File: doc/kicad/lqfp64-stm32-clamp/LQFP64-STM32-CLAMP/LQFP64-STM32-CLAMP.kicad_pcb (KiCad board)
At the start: 2 copper layers, 11 parts, among them J0 Conn_01x01, J1 Conn_01x16, J2 Conn_01x16, J3 Conn_01x16, J4 Conn_01x16, J5 Conn_01x12, J6 Conn_01x12, J7 Conn_01x12, J8 Conn_01x12, U1 STM32F030RCTx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

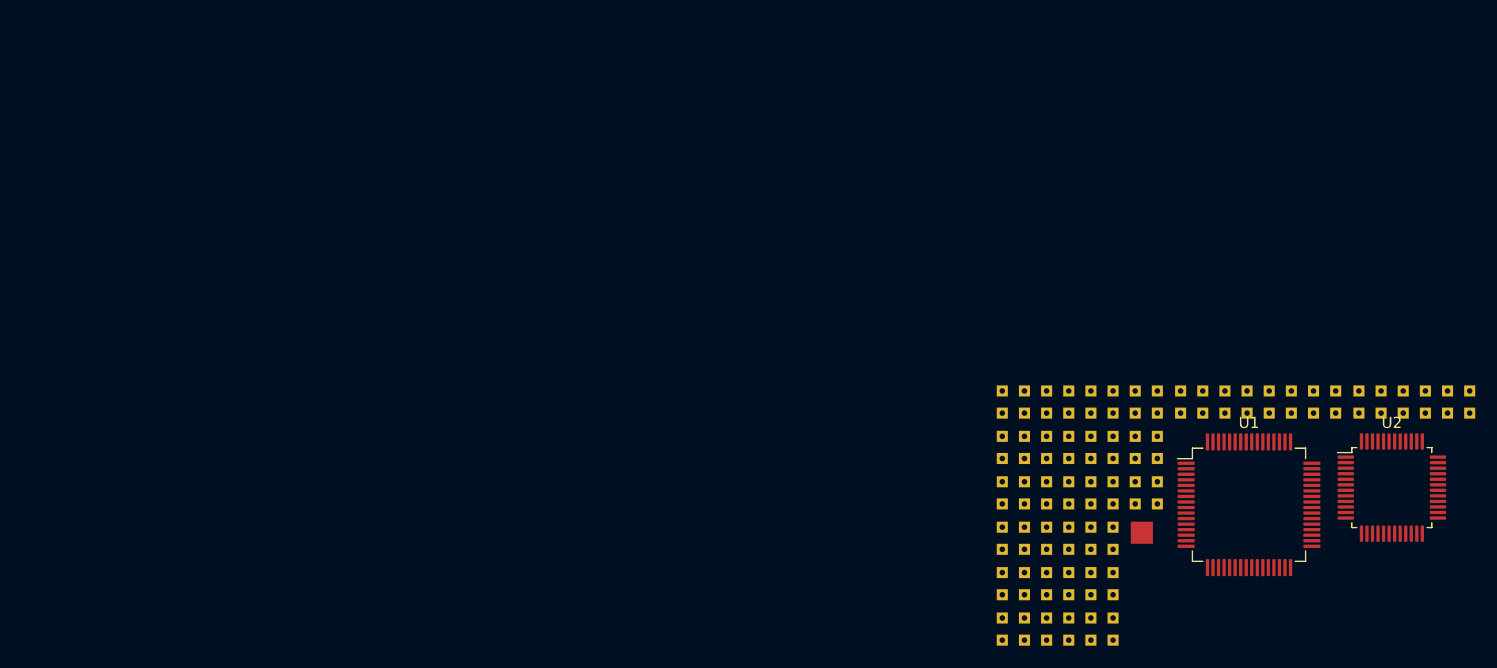
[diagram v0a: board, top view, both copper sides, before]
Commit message: doc/kicad: LQFP64-STM32-CLAMP PCB layout
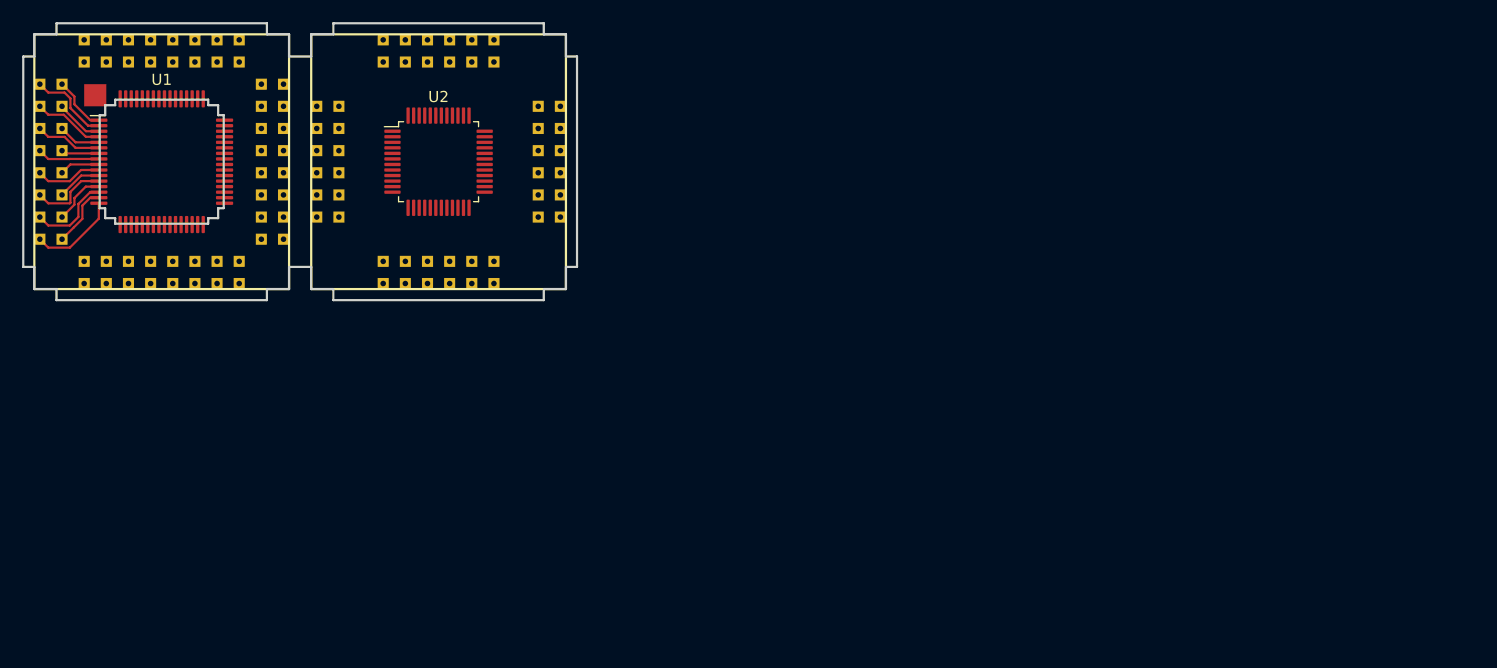
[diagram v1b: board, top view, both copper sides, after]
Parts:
- moved U1 102.9 mm to (53.0, 57.0)
- moved J0 102.4 mm to (47.0, 51.0)
- moved J1 95.4 mm to (43.0, 57.0), turned to 270 degrees
- moved J4 92.0 mm to (53.0, 47.0), turned to 180 degrees
- moved J3 91.6 mm to (63.0, 57.0), turned to 90 degrees
- moved U2 91.0 mm to (78.0, 57.0)
- moved J2 84.4 mm to (53.0, 67.0)
- moved J7 81.1 mm to (88.0, 57.0), turned to 90 degrees
- moved J8 76.5 mm to (78.0, 47.0), turned to 180 degrees
- moved J5 74.2 mm to (68.0, 57.0), turned to 270 degrees
- moved J6 62.6 mm to (78.0, 67.0)
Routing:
- net /P114: track 0.00 -> 8.32 mm
- net /P116: track 0.00 -> 8.12 mm
- net /P102: track 0.00 -> 7.39 mm
- net /P112: track 0.00 -> 7.05 mm
- net /P104: track 0.00 -> 6.46 mm
- net /P110: track 0.00 -> 6.06 mm
- net /P106: track 0.00 -> 6.05 mm
- net /P108: track 0.00 -> 5.64 mm
- net /P115: track 0.00 -> 5.58 mm
- net /P101: track 0.00 -> 5.29 mm
- net /P113: track 0.00 -> 4.82 mm
- net /P103: track 0.00 -> 4.31 mm
- net /P111: track 0.00 -> 4.06 mm
- net /P105: track 0.00 -> 3.86 mm
- net /P109: track 0.00 -> 3.64 mm
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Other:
- board outline added: 50 x 25 mm
